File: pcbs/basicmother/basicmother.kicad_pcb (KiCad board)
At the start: 2 copper layers, 61 parts, among them IC1 ATMEGA88-P, IC2 DRV8843, P1 DIL16, P2 CONN_02X05, P3 CONN_02X03, P4 CONN_01X02, P5 CONN_01X02, P6 CONN_01X02, P7 CONN_01X02, P8 CONN_01X02, P9 CONN_01X02, U1 ZIGBIT_DUAL_DIP, U2 MBED, U3 PTN4050, U4 LMZ12002, U5 LM4950TS, U6 LM4950TS, X1 18.432 MHz

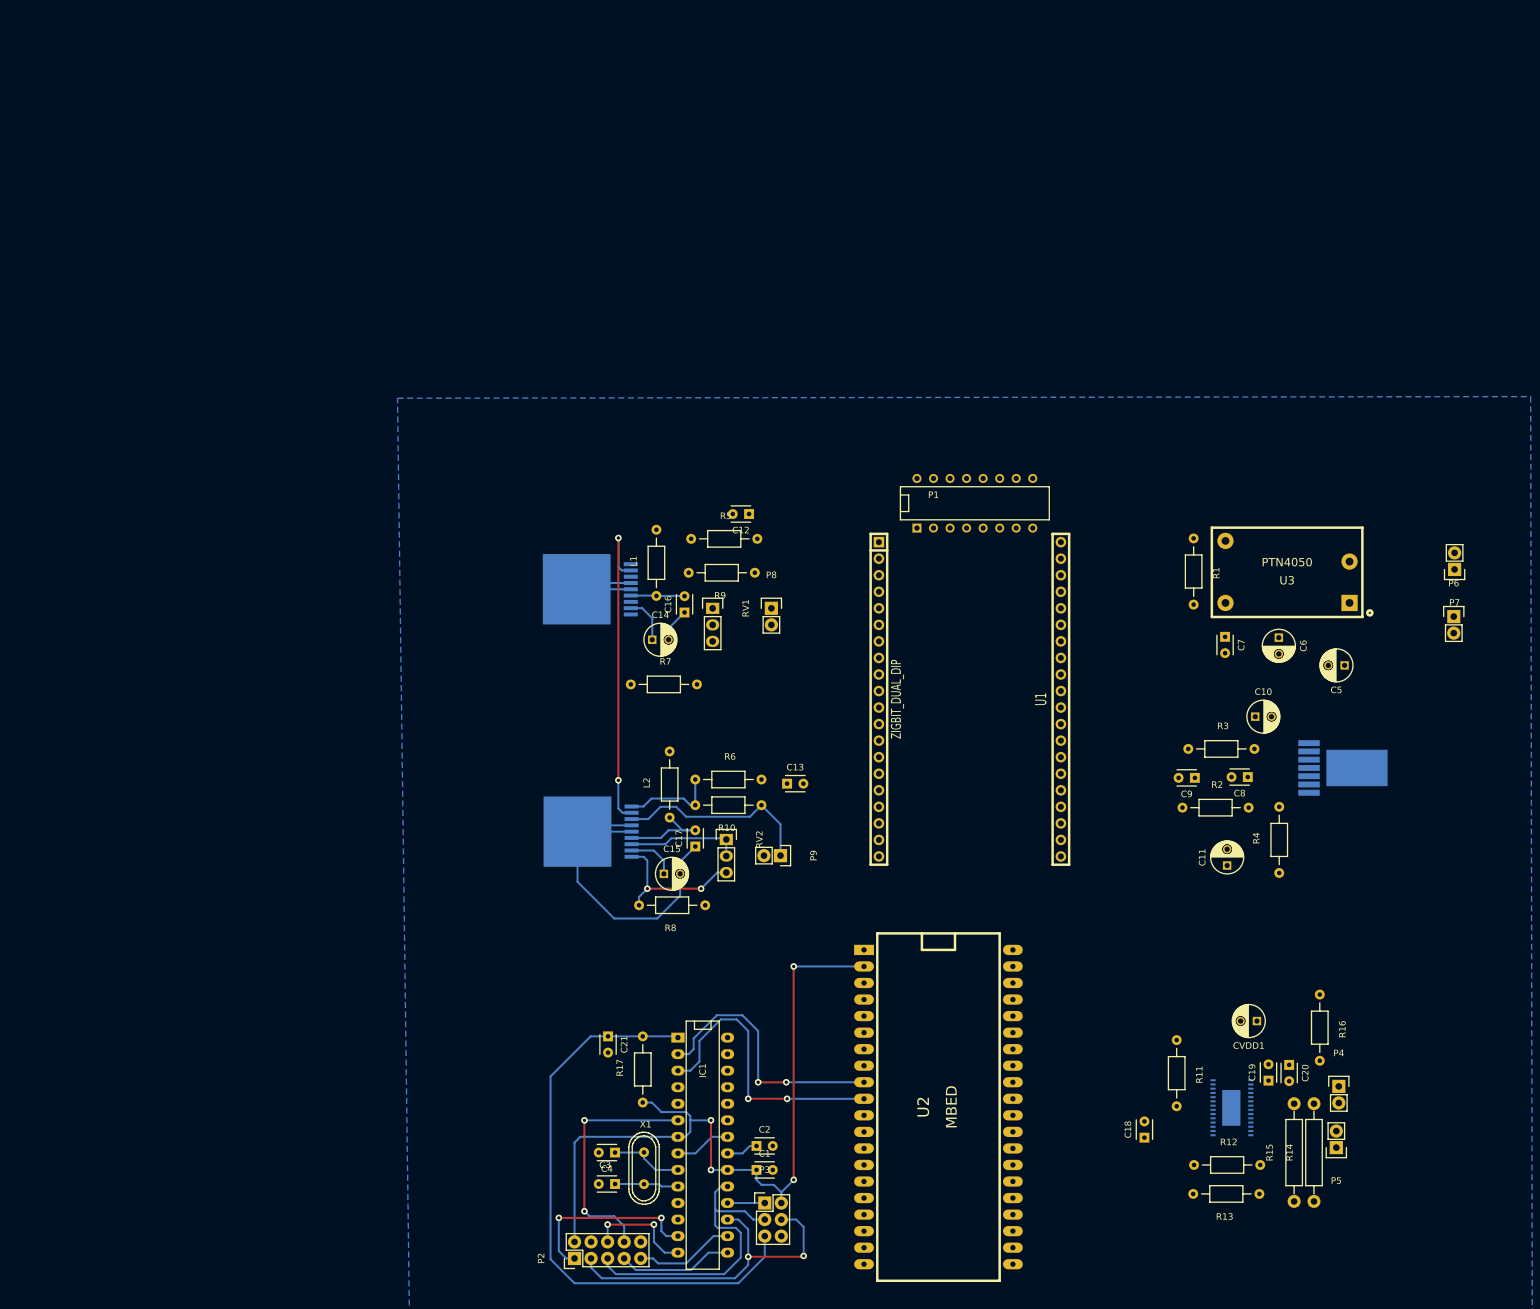
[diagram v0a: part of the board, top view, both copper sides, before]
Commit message: saque el micro para el control de los ojitos y lo pase a una placa aparte, ademas agregue un doble microfono
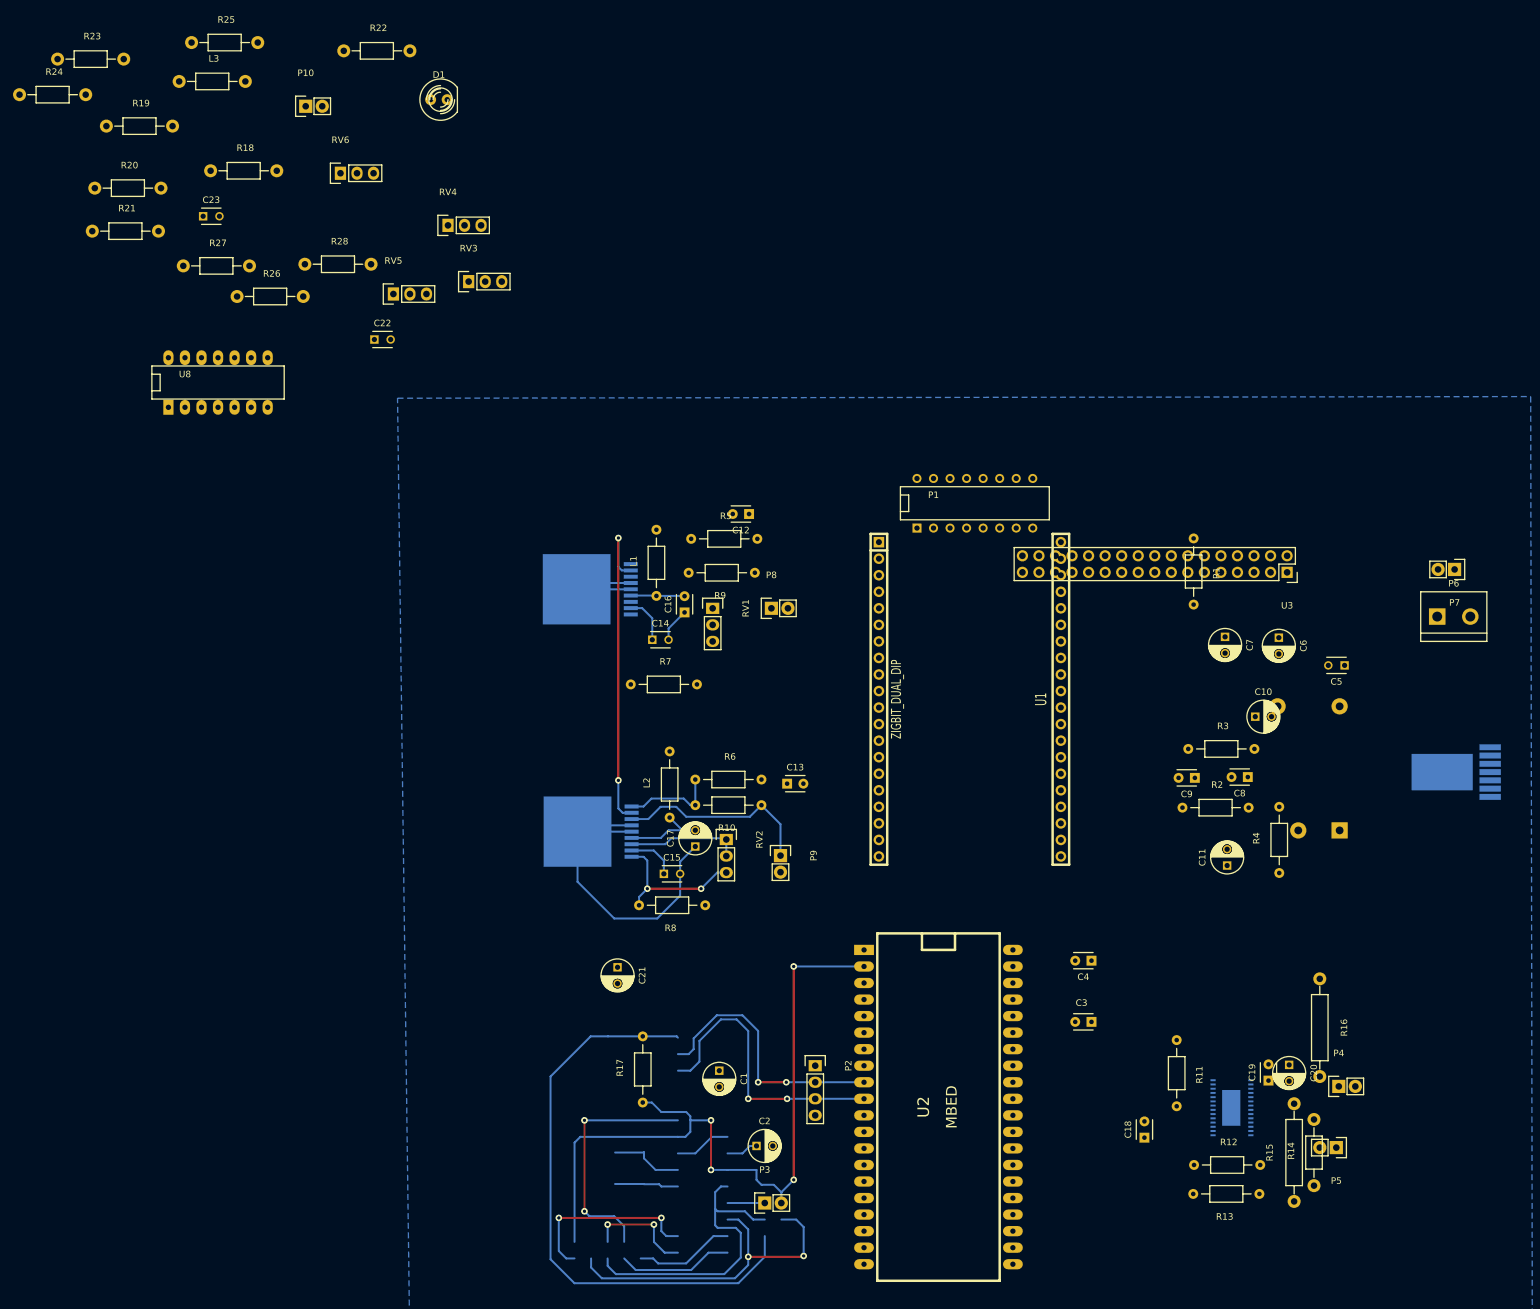
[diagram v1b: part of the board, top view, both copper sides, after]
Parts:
- removed CVDD1: 330 uF, Capacitors_ThroughHole:C_Radial_D5_L6_P2.5
- removed IC2: DRV8843, Popurri_CDR:HTSSOP28
- removed X1: 18.432 MHz, Crystals:Crystal_HC49-U_Vertical
- added C22: 5.6n, Capacitors_ThroughHole:C_Disc_D3_P2.5, F.Cu at (5.71, 15.0)
- added C23: 3.3n, Capacitors_ThroughHole:C_Disc_D3_P2.5, F.Cu at (-20.6, -3.94)
- added D1: LED, LEDs:LED-5MM, F.Cu at (15.6, -21.8)
- added L3: 1uH, Resistors_ThroughHole:Resistor_Horizontal_RM10mm, F.Cu at (-19.2, -24.6)
- added P10: mic_conn, Socket_Strips:Socket_Strip_Straight_1x02, F.Cu at (-4.83, -20.8)
- added R18: 2.2k, Resistors_ThroughHole:Resistor_Horizontal_RM10mm, F.Cu at (-14.4, -10.9)
- added R19: 2.2k, Resistors_ThroughHole:Resistor_Horizontal_RM10mm, F.Cu at (-30.4, -17.8)
- added R20: 10k, Resistors_ThroughHole:Resistor_Horizontal_RM10mm, F.Cu at (-32.1, -8.26)
- added R21: 47k, Resistors_ThroughHole:Resistor_Horizontal_RM10mm, F.Cu at (-32.5, -1.65)
- added R22: 10k, Resistors_ThroughHole:Resistor_Horizontal_RM10mm, F.Cu at (6.10, -29.3)
- added R23: 10k, Resistors_ThroughHole:Resistor_Horizontal_RM10mm, F.Cu at (-37.8, -28.1)
- added R24: 10k, Resistors_ThroughHole:Resistor_Horizontal_RM10mm, F.Cu at (-43.7, -22.6)
- added R25: 10k, Resistors_ThroughHole:Resistor_Horizontal_RM10mm, F.Cu at (-17.3, -30.6)
- added R26: 10k, Resistors_ThroughHole:Resistor_Horizontal_RM10mm, F.Cu at (-10.3, 8.38)
- added R27: 10k, Resistors_ThroughHole:Resistor_Horizontal_RM10mm, F.Cu at (-18.5, 3.68)
- added R28: 10k, Resistors_ThroughHole:Resistor_Horizontal_RM10mm, F.Cu at (0.13, 3.43)
- added RV3: 100k, Socket_Strips:Socket_Strip_Straight_1x03, F.Cu at (20.2, 6.10)
- added RV4: 100k, Socket_Strips:Socket_Strip_Straight_1x03, F.Cu at (17.0, -2.54)
- added RV5: 100k, Socket_Strips:Socket_Strip_Straight_1x03, F.Cu at (8.64, 8.00)
- added RV6: 100k, Socket_Strips:Socket_Strip_Straight_1x03, F.Cu at (0.51, -10.5)
- added U7: LM4950TS, Popurri_CDR:TO-263, B.Cu at (45.1, 53.3)
- added U8: LM324N, Sockets_DIP:DIP-14__300_ELL, F.Cu at (-18.3, 21.6)
- C1, C2, C20: value 100n -> 100u; footprint Capacitors_ThroughHole:C_Disc_D3_P2.5 -> Capacitors_ThroughHole:C_Radial_D5_L6_P2.5
- C10: value 100u -> 10u
- C12, C13: value 390n -> 1u
- C14: value 10u -> 100n; footprint Capacitors_ThroughHole:C_Radial_D5_L6_P2.5 -> Capacitors_ThroughHole:C_Disc_D3_P2.5
- C15: value 10u -> 10n; footprint Capacitors_ThroughHole:C_Radial_D5_L6_P2.5 -> Capacitors_ThroughHole:C_Disc_D3_P2.5
- C16: value 1u -> 100n
- C17: value 1u -> 330 uF; footprint Capacitors_ThroughHole:C_Disc_D3_P2.5 -> Capacitors_ThroughHole:C_Radial_D5_L6_P2.5
- C18: value 100n -> 1u
- C19: value 10n -> 10u
- C21, C7: value 100n -> 10u; footprint Capacitors_ThroughHole:C_Disc_D3_P2.5 -> Capacitors_ThroughHole:C_Radial_D5_L6_P2.5
- C3: value 22n -> 100n
- C5: value 100u -> 22n; footprint Capacitors_ThroughHole:C_Radial_D5_L6_P2.5 -> Capacitors_ThroughHole:C_Disc_D3_P2.5
- C8, C9: value 22n -> 390n
- IC1: value ATMEGA88-P -> DRV8843; footprint Sockets_DIP:DIP-28__300 -> Popurri_CDR:HTSSOP28; moved to B.Cu
- L1, L2: value 1 uH -> 1uH
- P1: value DIL16 -> ZIGBIT_DIP
- P2: value CONN_02X05 -> Eyes-comm; footprint Pin_Headers:Pin_Header_Straight_2x05 -> Socket_Strips:Socket_Strip_Straight_1x04
- P3: value CONN_02X03 -> L-MOTOR; footprint Pin_Headers:Pin_Header_Straight_2x03 -> Socket_Strips:Socket_Strip_Straight_1x02
- P4: value CONN_01X02 -> R-MOTOR; footprint Pin_Headers:Pin_Header_Straight_1x02 -> Socket_Strips:Socket_Strip_Straight_1x02
- P5: value CONN_01X02 -> SWITCH; footprint Pin_Headers:Pin_Header_Straight_1x02 -> Socket_Strips:Socket_Strip_Straight_1x02
- P6: value CONN_01X02 -> BATT; footprint Pin_Headers:Pin_Header_Straight_1x02 -> Connect:bornier2
- P7: value CONN_01X02 -> SPK1; footprint Pin_Headers:Pin_Header_Straight_1x02 -> Socket_Strips:Socket_Strip_Straight_1x02
- P8: value CONN_01X02 -> SPK2; footprint Pin_Headers:Pin_Header_Straight_1x02 -> Socket_Strips:Socket_Strip_Straight_1x02
- P9: value CONN_01X02 -> mic_conn; footprint Pin_Headers:Pin_Header_Straight_1x02 -> Socket_Strips:Socket_Strip_Straight_1x02
- R1: value 1.35k -> 1k
- R11: value 10k -> 22k
- R14: value .47 -> 10k; footprint Resistors_ThroughHole:Resistor_Horizontal_RM15mm -> Resistors_ThroughHole:Resistor_Horizontal_RM10mm
- R16: value 1M -> .47; footprint Resistors_ThroughHole:Resistor_Horizontal_RM10mm -> Resistors_ThroughHole:Resistor_Horizontal_RM15mm
- R17: value 10k -> 1M
- R2: value 1.07k -> 1.35k
- R3: value 5.62k -> 1.07k
- R4: value 100k -> 5.62k
- R5: value 22k -> 100k
- RV1, RV2: value POT -> 50k
- U3: value PTN4050 -> bluetooth-mod; footprint Power_CDR:PTN04050C-EUU -> Socket_Strips:Socket_Strip_Straight_2x17
- U4: value LMZ12002 -> PTN4050; footprint Popurri_CDR:PFM7 -> Power_CDR:PTN04050C-EUU
- U5: value LM4950TS -> LMZ12002; footprint Popurri_CDR:TO-263 -> Popurri_CDR:PFM7
- moved U5 134.9 mm to (177.0, 81.4)
- moved IC1 81.4 mm to (137.3, 133.0)
- moved C4 78.9 mm to (115.8, 110.4)
- moved C3 77.3 mm to (115.8, 119.8)
- moved P2 47.3 mm to (73.4, 126.5), turned to 270 degrees
- moved C1 16.3 mm to (58.7, 127.3), turned to 270 degrees
- moved C21 10.7 mm to (43.1, 111.4)
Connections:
- C10 pad 1: +5V -> Net-(C10-Pad1)
- C11 pad 1: +15V -> Net-(C11-Pad1)
- C12 pad 1: Net-(C12-Pad1) -> GND
- C12 pad 2: /sound/In -> Net-(C12-Pad2)
- C13 pad 1: Net-(C13-Pad1) -> GND
- C13 pad 2: /sound/In -> Net-(C13-Pad2)
- C14 pad 1: Net-(C14-Pad1) -> /motordrv/INT33
- C15 pad 2: GND -> Net-(C15-Pad2)
- C16 pad 1: GND -> +15V
- C17 pad 1: GND -> +15V
- C17 pad 2: Net-(C17-Pad2) -> GND
- C18 pad 1: /motordrv/INT33 -> /microfono/VCC2
- C2 pad 1: Net-(C2-Pad1) -> +12V
- C20 pad 1: +15V -> Net-(C20-Pad1)
- C21 pad 1: /RST -> Net-(C21-Pad1)
- C3 pad 1: Net-(C3-Pad1) -> +12V
- C5 pad 1: +5V -> Net-(C5-Pad1)
- C5 pad 2: GND -> +5V
- C6 pad 1: +12V -> +5V
- C7 pad 1: +12V -> +15V
- C8 pad 2: GND -> /sound/In
- C9 pad 2: +5V -> /sound/In
- IC1 pad 1: /RST -> Net-(C15-Pad2)
- IC1 pad 10: Net-(C3-Pad1) -> /motordrv/MOUT_B1
- IC1 pad 11: (no net) -> +15V
- IC1 pad 12: (no net) -> Net-(IC1-Pad12)
- IC1 pad 13: /VPRG -> Net-(IC1-Pad12)
- IC1 pad 14: /GSCLK -> GND
- IC1 pad 15: /XLAT -> /motordrv/INT33
- IC1 pad 16: /BLANK -> /motordrv/~RESET
- IC1 pad 17: /MOSI -> /motordrv/~SLEEP
- IC1 pad 18: /MISO -> /motordrv/~FAULT
- IC1 pad 19: /SCK -> Net-(IC1-Pad19)
- IC1 pad 2: /EYE-RX -> Net-(C15-Pad1)
- IC1 pad 20: +5V -> /motordrv/IN_A2
- IC1 pad 21: Net-(C2-Pad1) -> /motordrv/IN_A1
- IC1 pad 22: GND -> /motordrv/IN_B1
- IC1 pad 23: (no net) -> /motordrv/IN_B2
- IC1 pad 24: (no net) -> GND
- IC1 pad 25: (no net) -> GND
- IC1 pad 26: (no net) -> GND
- IC1 pad 27: (no net) -> GND
- IC1 pad 28: (no net) -> GND
- IC1 pad 3: /EYE-TX -> Net-(C16-Pad2)
- IC1 pad 4: (no net) -> +15V
- IC1 pad 5: (no net) -> /motordrv/MOUT_A1
- IC1 pad 6: /DCPRG -> Net-(IC1-Pad6)
- IC1 pad 7: +5V -> /motordrv/MOUT_A2
- IC1 pad 8: GND -> /motordrv/MOUT_B2
- IC1 pad 9: Net-(C4-Pad1) -> Net-(IC1-Pad9)
- L1 pad 1: Net-(C16-Pad2) -> Net-(C12-Pad2)
- L2 pad 1: Net-(C17-Pad2) -> Net-(C13-Pad2)
- P2 pad 1: /VPRG -> +5V
- P2 pad 2: +5V -> /EYE-RX
- P2 pad 3: /MOSI -> /EYE-TX
- P2 pad 4: (no net) -> GND
- P3 pad 1: /MISO -> /motordrv/MOUT_A1
- P3 pad 2: +5V -> /motordrv/MOUT_A2
- P4 pad 1: /motordrv/MOUT_A1 -> /motordrv/MOUT_B1
- P4 pad 2: /motordrv/MOUT_A2 -> /motordrv/MOUT_B2
- P5 pad 1: /motordrv/MOUT_B1 -> +BATT
- P5 pad 2: /motordrv/MOUT_B2 -> +15V
- P6 pad 2: +15V -> GND
- P7 pad 1: +BATT -> Net-(P7-Pad1)
- P7 pad 2: GND -> Net-(P7-Pad2)
- P9 pad 1: Net-(P9-Pad1) -> Net-(C19-Pad1)
- P9 pad 2: Net-(P9-Pad2) -> GND
- R1 pad 2: GND -> Net-(D1-Pad1)
- R10 pad 1: Net-(P9-Pad1) -> Net-(P7-Pad1)
- R11 pad 1: +5V -> Net-(P8-Pad1)
- R11 pad 2: Net-(IC2-Pad19) -> Net-(R11-Pad2)
- R12 pad 1: /motordrv/INT33 -> +5V
- R12 pad 2: Net-(IC2-Pad12) -> Net-(IC1-Pad19)
- R13 pad 1: Net-(IC2-Pad12) -> /motordrv/INT33
- R13 pad 2: GND -> Net-(IC1-Pad12)
- R14 pad 1: GND -> Net-(IC1-Pad12)
- R14 pad 2: Net-(IC2-Pad6) -> GND
- R15 pad 2: Net-(IC2-Pad9) -> Net-(IC1-Pad6)
- R16 pad 1: +15V -> GND
- R16 pad 2: Net-(C20-Pad2) -> Net-(IC1-Pad9)
- R17 pad 1: +5V -> +15V
- R17 pad 2: /RST -> Net-(C16-Pad2)
- R2 pad 1: Net-(C9-Pad1) -> Net-(R2-Pad1)
- R3 pad 1: +5V -> Net-(C5-Pad1)
- R3 pad 2: Net-(C9-Pad1) -> GND
- R4 pad 1: +15V -> +5V
- R4 pad 2: Net-(R4-Pad2) -> Net-(C5-Pad1)
- R5 pad 1: Net-(R5-Pad1) -> +15V
- R5 pad 2: Net-(C12-Pad1) -> Net-(R5-Pad2)
- R6 pad 2: Net-(C13-Pad1) -> Net-(C8-Pad1)
- R7 pad 1: Net-(P8-Pad1) -> Net-(R11-Pad2)
- R7 pad 2: Net-(R7-Pad2) -> Net-(C9-Pad1)
- R8 pad 1: Net-(P9-Pad1) -> Net-(P7-Pad1)
- R9 pad 2: Net-(R5-Pad1) -> Net-(R9-Pad2)
- RV1 pad 1: Net-(P8-Pad2) -> Net-(P7-Pad2)
- RV1 pad 2: Net-(P8-Pad2) -> Net-(P7-Pad2)
- RV1 pad 3: Net-(R7-Pad2) -> Net-(R8-Pad2)
- RV2 pad 1: Net-(P9-Pad2) -> Net-(P8-Pad2)
- RV2 pad 2: Net-(P9-Pad2) -> Net-(P8-Pad2)
- RV2 pad 3: Net-(R8-Pad2) -> Net-(R9-Pad2)
- U1 pad 22: Net-(U1-Pad22) -> +3V3
- U2 pad 15: (no net) -> /microfono/OUT
- U2 pad 27: (no net) -> /TXDBT
- U2 pad 28: (no net) -> /RXDBT
- U2 pad 40: Net-(U1-Pad22) -> +3V3
- U3 pad 1: GND -> /TXDBT
- U3 pad 2: +5V -> /RXDBT
- U3 pad 3: Net-(R1-Pad1) -> (no net)
- U3 pad 4: +12V -> (no net)
- U4 pad 1: +15V -> GND
- U4 pad 2: Net-(R4-Pad2) -> +5V
- U4 pad 3: (no net) -> Net-(R2-Pad1)
- U4 pad 4: GND -> +12V
- U5 pad 1: Net-(R5-Pad1) -> +15V
- U5 pad 2: /sound/~SHD -> Net-(R5-Pad2)
- U5 pad 3: Net-(P8-Pad1) -> (no net)
- U5 pad 5: GND -> Net-(C4-Pad1)
- U5 pad 6: Net-(C16-Pad2) -> Net-(C5-Pad1)
- U5 pad 7: Net-(P8-Pad2) -> +5V
- U6 pad 3: Net-(P9-Pad1) -> Net-(P7-Pad1)
- U6 pad 6: Net-(C17-Pad2) -> Net-(C12-Pad2)
- U6 pad 7: Net-(P9-Pad2) -> Net-(P7-Pad2)
- U6 pad 8: Net-(C15-Pad1) -> Net-(C10-Pad1)
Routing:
- net (no net): track 0.00 -> 246.4 mm, vias 0 -> 8
- net /RST: track 89.5 -> 0.00 mm
- net Net-(C16-Pad2): track 8.29 -> 89.6 mm
- net /MOSI: track 53.2 -> 0.00 mm, vias 2 -> 0
- net /SCK: track 47.0 -> 0.00 mm
- net /DCPRG: track 37.8 -> 0.00 mm, vias 2 -> 0
- net Net-(P9-Pad1): track 31.0 -> 0.00 mm
- net /VPRG: track 28.6 -> 0.00 mm, vias 2 -> 0
- net Net-(P7-Pad1): track 0.00 -> 26.2 mm
- net /XLAT: track 17.7 -> 0.00 mm
- net Net-(P9-Pad2): track 17.5 -> 0.00 mm
- net /GSCLK: track 16.8 -> 0.00 mm, vias 2 -> 0
- net +15V: track 0.00 -> 15.6 mm
- net /BLANK: track 15.4 -> 0.00 mm
- net Net-(C17-Pad2): track 15.0 -> 0.00 mm
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
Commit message: primera version del pcb de la placa principal, falta verificar footprints
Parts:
- C19: footprint Capacitors_ThroughHole:C_Disc_D3_P2.5 -> Capacitors_ThroughHole:C_Radial_D5_L6_P2.5
- U4: moved to F.Cu
- moved R25 226.2 mm to (131.8, 139.4), turned to 180 degrees
- moved R24 223.8 mm to (105.2, 144.5), turned to 180 degrees
- moved R23 211.7 mm to (105.2, 128.0)
- moved R27 206.8 mm to (126.7, 150.9), turned to 180 degrees
- moved C23 205.3 mm to (129.9, 135.6), turned to 180 degrees
- moved R20 202.6 mm to (105.2, 140.7), turned to 180 degrees
- moved RV6 202.2 mm to (131.8, 143.3), turned to 180 degrees
- moved P10 197.8 mm to (95.6, 149.6), turned to 180 degrees
- moved R19 196.4 mm to (89.9, 137.5), turned to 270 degrees
- moved R26 195.4 mm to (126.7, 147.7), turned to 180 degrees
- moved R21 195.3 mm to (105.2, 136.9)
- moved R22 189.2 mm to (105.2, 131.8)
- moved L3 188.5 mm to (102.0, 119.8)
- moved R28 183.9 mm to (131.8, 131.8), turned to 180 degrees
- moved U8 178.1 mm to (118.5, 135.6), turned to 270 degrees
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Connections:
- U2 pad 11: /sound/~SHD -> (no net)
- U2 pad 19: /motordrv/~RESET -> /motordrv/~SLEEP
- U2 pad 20: /motordrv/~SLEEP -> /motordrv/~RESET
- U2 pad 25: /motordrv/IN_A2 -> /motordrv/IN_A1
- U2 pad 26: /motordrv/IN_A1 -> /motordrv/IN_A2
- U2 pad 30: (no net) -> /sound/~SHD
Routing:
- net (no net): track 246.4 -> 0.00 mm, vias 8 -> 0
- net +3V3: track 0.00 -> 130.3 mm, vias 0 -> 2
- net +5V: track 105.6 -> 225.8 mm, vias 4 -> 2
- net +15V: track 15.6 -> 109.6 mm, vias 0 -> 2
- net +12V: track 4.92 -> 84.6 mm, vias 0 -> 2
- net Net-(C16-Pad2): track 89.6 -> 16.3 mm
- net /microfono/VCC2: track 0.00 -> 61.1 mm, vias 0 -> 2
- net /sound/In: track 0.00 -> 52.3 mm
- net /ZIGBIT_RESET: track 0.00 -> 47.7 mm, vias 0 -> 2
- net /DIPSW_7: track 0.00 -> 45.9 mm
- net /microfono/OUT: track 0.00 -> 45.7 mm, vias 0 -> 2
- net /DIPSW_8: track 0.00 -> 43.2 mm
- net Net-(P8-Pad1): track 0.00 -> 41.9 mm
- net /RXDBT: track 0.00 -> 39.6 mm
- net /motordrv/IN_A2: track 0.00 -> 39.2 mm
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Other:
- rule via_min_drill: 0.4572 -> 0.5

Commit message: actualizo las 3 placas, revisar y mandar a fabricar
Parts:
- added P11: BATT, Popurri_CDR:molex_2_recto, F.Cu at (203.1, 59.3)
- added REF**: 1pin, Connect:1pin, F.Cu at (87.4, 105.5)
- added REF**: 1pin, Connect:1pin, F.Cu at (111.9, 40.4)
- added REF**: 1pin, Connect:1pin, F.Cu at (205.8, 38.4)
- added REF**: 1pin, Connect:1pin, F.Cu at (106.1, 90.0)
- added REF**: 1pin, Connect:1pin, F.Cu at (203.4, 145.6)
- added REF**: 1pin, Connect:1pin, F.Cu at (203.3, 126.9)
- C12, C13, C18: footprint Capacitors_ThroughHole:C_Disc_D3_P2.5 -> Capacitors_ThroughHole:C_Rect_L18_W5_P15
- C4, C5: footprint Capacitors_ThroughHole:C_Disc_D3_P2.5 -> Capacitors_ThroughHole:C_Rect_L7_W2_P5
- moved C13 26.9 mm to (125.5, 59.9), turned to 0 degrees
- moved C12 26.1 mm to (125.5, 53.8), turned to 0 degrees
- moved C1 13.7 mm to (205.1, 45.2), turned to 270 degrees
- moved C18 6.56 mm to (107.1, 114.9), turned to 180 degrees
- moved R2 6.25 mm to (185.5, 53.5)
- moved U4 4.23 mm to (189.5, 43.2)
- moved C3 3.83 mm to (172.3, 39.1)
- moved C2 3.20 mm to (172.3, 46.7)
- moved R1 3.18 mm to (94.4, 71.2)
- moved D1 3.17 mm to (94.4, 86.4)
- moved C5 2.43 mm to (174.6, 65.3), turned to 0 degrees
- moved R8 2.03 mm to (150.4, 55.1)
- moved RV3 1.33 mm to (116.0, 121.0)
- moved R4 0.90 mm to (176.7, 62.0)
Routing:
- net GND: track 40.5 -> 150.3 mm
- net Net-(C13-Pad2): track 7.05 -> 25.0 mm, vias 0 -> 2
- net +BATT: track 6.80 -> 24.3 mm
- net Net-(C12-Pad2): track 7.12 -> 22.6 mm, vias 0 -> 2
- net /microfono/VCC2: track 61.1 -> 68.1 mm
- net Net-(R2-Pad1): track 15.9 -> 19.0 mm
- net +12V: track 84.6 -> 81.7 mm
- net Net-(P7-Pad1): track 39.5 -> 37.6 mm
- net /sound/~SHD: track 69.7 -> 71.2 mm
- net Net-(C5-Pad1): track 15.8 -> 17.2 mm
- net /microfono/Vref: track 29.3 -> 30.6 mm
- net Net-(R8-Pad2): track 21.0 -> 19.9 mm
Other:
- board outline added: 125.7 x 121 mm
- net class Default: via_dia 1.016 -> 1.778
- board text added: "Marciano - MotherBoard"

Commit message: cambios hechos en las placas
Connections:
- REF** pad 1: (no net) -> GND
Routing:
- added copper zone on F.Cu, net GND
